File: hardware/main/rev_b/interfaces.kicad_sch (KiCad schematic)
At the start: 12 parts, among them U50 TCAN3413DR, U51 MCP2518FD-H/QBB, Y50 40MHz ABM8G

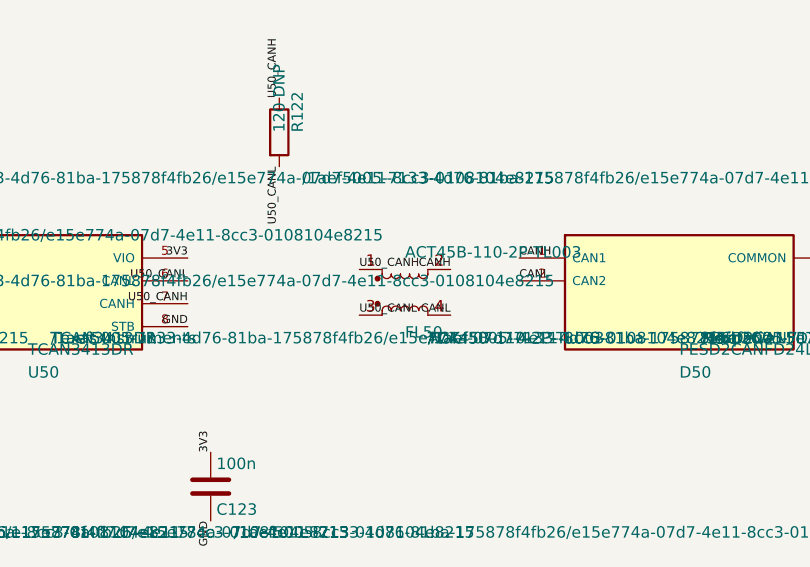
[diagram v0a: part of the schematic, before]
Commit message: revert ESC to front-side-only placement from 325f93b; main board CANL routing + ACT45B pinout fix
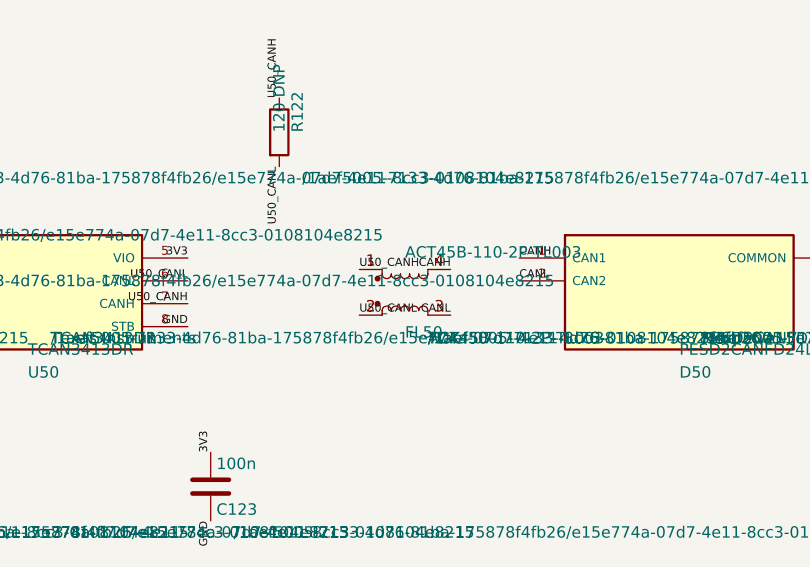
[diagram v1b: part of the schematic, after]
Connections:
- net CANH: now also FL50.4; no longer FL50.2
- net CANL: now also FL50.3; no longer FL50.4
- net U50_CANL: now also FL50.2; no longer FL50.3
